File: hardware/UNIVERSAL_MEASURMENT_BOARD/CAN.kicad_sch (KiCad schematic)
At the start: 12 parts, among them U5 ADM3055EBRIZ-RL

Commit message: continued
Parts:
- removed FB2: FerriteBead_Small, symbol Device:FerriteBead_Small
- added C61: 47uF, symbol Device:C_Small
- added C67: 4.7nF/Y2, Samacsys:CAPC5728X280N, symbol Samacsys_kicad_sym:S252B222K502CT
- added FB1, FB3, FB4: 2K@100MHz, symbol Device:FerriteBead_Small
- added TP1: C5V, symbol Connector:TestPoint
- added TP2: C3V, symbol Connector:TestPoint
- C58: renamed from C13; value 220nF -> 47uF
- C59: renamed from C14; value 10uF -> 47uF
- C60: renamed from C17; value 10uF -> 47uF
- FB2: renamed from FB1; value FerriteBead_Small -> 2K@100MHz
- R14: renamed from R2; value R -> 100kR
- renumbered C18 to C62, C19 to C63, C20 to C64, C15 to C65, C16 to C66, U5 to U14
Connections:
- net +3V3: now also FB3.2; no longer C64.1, U14.4 (VIO)
- net +5V: now also FB1.2; no longer C62.1, U14.3 (VCC)
- net BUS_GND: now also C67.1, FB4.2
- net GND: now also U14.9 (AUXIN), C61.2, C67.2
- net at C58.2, U14.18 (GNDISO), U14.20 (GNDISO_2): now also FB4.1
- net CAN_STB: now reaches U14.8 (STBY)
- new net: C61.1, C62.1, FB1.1, TP1.1, U14.3 (VCC)
- new net: C64.1, FB3.1, TP2.1, U14.4 (VIO)
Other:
- note added: "ISOLATED"
- note added: "NON ISOLATED"
- note removed: "Co z VISO"
- company: (none) -> PUT Motorsport Formula Student team
- title: (none) -> Universal Measurment Board
- moved on the sheet: C58, C59, C60, C62, C63, C64, C65, C66, FB2, R14

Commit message: final schematic review corrections
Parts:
- added TP3: CVISO, symbol Connector:TestPoint
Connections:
- net VISO: now also TP3.1
- net +5V renamed +5V0A
- net RX renamed CAN_RX
- net TX renamed CAN_TX
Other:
- moved on the sheet: C58, C59, C60, C61, C62, C63, C64, C65, C66, C67, FB1, FB2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

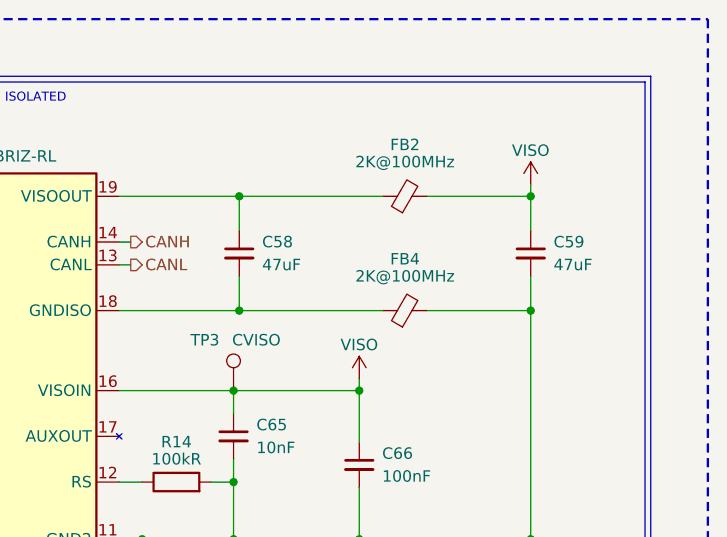
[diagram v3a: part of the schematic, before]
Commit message: added footprints
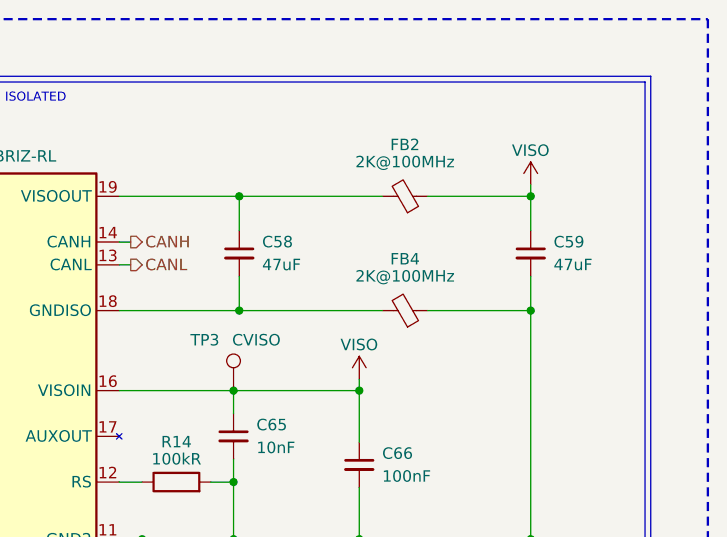
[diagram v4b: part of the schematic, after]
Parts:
- C58, C59, C60, C61, C62, C63, C64, C65, C66: footprint (none) -> Capacitor_SMD:C_0603_1608Metric
- C67: footprint Samacsys:CAPC5728X280N -> S252B222K502CT:CAPC5728X280N
- FB1, FB2, FB3, FB4: footprint (none) -> Inductor_SMD:L_0805_2012Metric
- R14: footprint (none) -> Resistor_SMD:R_0603_1608Metric
- TP1, TP2, TP3: footprint (none) -> TestPoint:TestPoint_Pad_D1.5mm
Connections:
- net BUS_GND: now also FB4.1; no longer FB4.2
- net VISO: now also FB2.1; no longer FB2.2
- net at C58.1, U14.19 (VISOOUT): now also FB2.2; no longer FB2.1
- net at C58.2, U14.18 (GNDISO), U14.20 (GNDISO_2): now also FB4.2; no longer FB4.1
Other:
- company: PUT Motorsport Formula Student team -> PUT Motorsport Formula Student Team
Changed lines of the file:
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@@
 		(title "Universal Measurment Board")
 		(date "2026-02-02")
-		(rev "1.7.14")
-		(company "PUT Motorsport Formula Student team")
+		(rev "1.7.15")
+		(company "PUT Motorsport Formula Student Team")
 		(comment 1 "Designed by Marcin Trzmiel under")
 	)
@@
 			)
 		)
-		(property "Footprint" ""
+		(property "Footprint" "Capacitor_SMD:C_0603_1608Metric"
 			(at 94.615 88.265 0)
 			(effects
@@
 			)
 		)
-		(property "Footprint" ""
+		(property "Footprint" "TestPoint:TestPoint_Pad_D1.5mm"
 			(at 146.05 69.215 0)
 			(effects
@@
 			)
 		)
-		(property "Footprint" ""
+		(property "Footprint" "TestPoint:TestPoint_Pad_D1.5mm"
 			(at 129.54 76.835 0)
 			(effects
@@
 	)
 	(symbol
-		(lib_id "Device:FerriteBead_Small")
-		(at 76.2 69.215 270)
-		(unit 1)
-		(exclude_from_sim no)
-		(in_bom yes)
-		(on_board yes)
-		(dnp no)
-		(property "Reference" "FB1"
-			(at 76.2 73.025 90)
-			(effects
-				(font
-					(size 1.27 1.27)
-				)
-			)
-		)
-		(property "Value" "2K@100MHz"
-			(at 76.2 74.93 90)
-			(effects
-				(font
-					(size 1.27 1.27)
-				)
-			)
-		)
-		(property "Footprint" ""
-			(at 76.2 67.437 90)
-			(effects
-				(font
-					(size 1.27 1.27)
-				)
-				(hide yes)
-			)
-		)
-		(property "Datasheet" "~"
-			(at 76.2 69.215 0)
-			(effects
-				(font
-					(size 1.27 1.27)
-				)
-				(hide yes)
-			)
-		)
-		(property "Description" "Ferrite bead, small symbol"
-			(at 76.2 69.215 0)
-			(effects
-				(font
-					(size 1.27 1.27)
-				)
-				(hide yes)
-			)
-		)
-		(pin "2"
-		)
-		(pin "1"
-		)
-		(instances
-			(project "UNIVERSAL_MEASURMENT_BOARD"
-				(path "/92c00310-4384-4ef3-9368-efad75526047/007c1dd5-a7d9-42e3-b7c2-f5a2b9d94f0b"
-					(reference "FB1")
-					(unit 1)
-				)
-			)
-		)
-	)
-	(symbol
 		(lib_id "Samacsys_kicad_sym:S252B222K502CT")
 		(at 164.465 118.745 180)
@@
 			)
 		)
-		(property "Footprint" "Samacsys:CAPC5728X280N"
+		(property "Footprint" "S252B222K502CT:CAPC5728X280N"
 			(at 155.575 22.555 0)
 			(effects
@@
 			)
 		)
-		(property "Datasheet" ""
+		(property "Datasheet" "https://4donline.ihs.com/images/VipMasterIC/IC/WATC/WATC-S-A0011771687/WATC-S-A0011771687-1.pdf?hkey=CECEF36DEECDED6468708AAF2E19C0C6"
 			(at 155.575 -77.445 0)
 			(effects
@@
 			)
 		)
-		(property "Footprint" ""
+		(property "Footprint" "Capacitor_SMD:C_0603_1608Metric"
 			(at 193.04 75.565 0)
 			(effects
@@
 	)
 	(symbol
-		(lib_id "Device:FerriteBead_Small")
-		(at 211.455 69.215 90)
-		(unit 1)
-		(exclude_from_sim no)
-		(in_bom yes)
-		(on_board yes)
-		(dnp no)
-		(property "Reference" "FB2"
-			(at 211.455 63.5 90)
-			(effects
-				(font
-					(size 1.27 1.27)
-				)
-			)
-		)
-		(property "Value" "2K@100MHz"
-			(at 211.455 65.405 90)
-			(effects
-				(font
-					(size 1.27 1.27)
-				)
-			)
-		)
-		(property "Footprint" ""
-			(at 211.455 70.993 90)
-			(effects
-				(font
-					(size 1.27 1.27)
-				)
-				(hide yes)
-			)
-		)
-		(property "Datasheet" "~"
-			(at 211.455 69.215 0)
-			(effects
-				(font
-					(size 1.27 1.27)
-				)
-				(hide yes)
-			)
-		)
-		(property "Description" "Ferrite bead, small symbol"
-			(at 211.455 69.215 0)
-			(effects
-				(font
-					(size 1.27 1.27)
-				)
-				(hide yes)
-			)
-		)
-		(pin "2"
-		)
-		(pin "1"
-		)
-		(instances
-			(project ""
-				(path "/92c00310-4384-4ef3-9368-efad75526047/007c1dd5-a7d9-42e3-b7c2-f5a2b9d94f0b"
-					(reference "FB2")
-					(unit 1)
-				)
-			)
-		)
-	)
-	(symbol
 		(lib_id "Device:C_Small")
 		(at 225.425 75.565 0)
@@
 			)
 		)
-		(property "Footprint" ""
+		(property "Footprint" "Capacitor_SMD:C_0603_1608Metric"
 			(at 225.425 75.565 0)
 			(effects
@@
 			)
 		)
-		(property "Footprint" ""
+		(property "Footprint" "Capacitor_SMD:C_0603_1608Metric"
 			(at 192.405 95.885 0)
 			(effects
@@
 	(symbol
 		(lib_id "Device:FerriteBead_Small")
-		(at 211.455 81.915 90)
+		(at 211.455 81.915 270)
+		(mirror x)
 		(unit 1)
 		(exclude_from_sim no)
@@
 			)
 		)
-		(property "Footprint" ""
+		(property "Footprint" "Inductor_SMD:L_0805_2012Metric"
 			(at 211.455 83.693 90)
 			(effects
@@
 			)
 		)
-		(property "Datasheet" "~"
+		(property "Datasheet" "https://www.mouser.pl/ProductDetail/Fair-Rite/2508052027Y1?qs=paL1wOLBYNcCgyNDp2sTMQ%3D%3D"
 			(at 211.455 81.915 0)
 			(effects
@@
 			)
 		)
-		(property "Footprint" ""
+		(property "Footprint" "Capacitor_SMD:C_0603_1608Metric"
 			(at 125.095 92.075 0)
 			(effects
@@
 			)
 		)
-		(property "Footprint" ""
+		(property "Footprint" "Resistor_SMD:R_0603_1608Metric"
 			(at 186.055 102.743 90)
 			(effects
@@
 			)
 		)
-		(property "Footprint" ""
+		(property "Footprint" "Inductor_SMD:L_0805_2012Metric"
 			(at 117.475 75.057 90)
 			(effects
@@
 			)
 		)
-		(property "Datasheet" "~"
+		(property "Datasheet" "https://www.mouser.pl/ProductDetail/Fair-Rite/2508052027Y1?qs=paL1wOLBYNcCgyNDp2sTMQ%3D%3D"
 			(at 117.475 76.835 0)
 			(effects
@@
 			)
 		)
-		(property "Footprint" ""
+		(property "Footprint" "Capacitor_SMD:C_0603_1608Metric"
 			(at 206.375 99.06 0)
 			(effects
@@
 			)
 		)
-		(property "Footprint" ""
+		(property "Footprint" "Capacitor_SMD:C_0603_1608Metric"
 			(at 68.58 88.265 0)
 			(effects
@@
 	)
 	(symbol
+		(lib_id "Device:FerriteBead_Small")
+		(at 211.455 69.215 270)
+		(mirror x)
+		(unit 1)
+		(exclude_from_sim no)
+		(in_bom yes)
+		(on_board yes)
+		(dnp no)
+		(property "Reference" "FB2"
+			(at 211.455 63.5 90)
+			(effects
+				(font
+					(size 1.27 1.27)
+				)
+			)
+		)
+		(property "Value" "2K@100MHz"
+			(at 211.455 65.405 90)
+			(effects
+				(font
+					(size 1.27 1.27)
+				)
+			)
+		)
+		(property "Footprint" "Inductor_SMD:L_0805_2012Metric"
+			(at 211.455 70.993 90)
+			(effects
+				(font
+					(size 1.27 1.27)
+				)
+				(hide yes)
+			)
+		)
+		(property "Datasheet" "https://www.mouser.pl/ProductDetail/Fair-Rite/2508052027Y1?qs=paL1wOLBYNcCgyNDp2sTMQ%3D%3D"
+			(at 211.455 69.215 0)
+			(effects
+				(font
+					(size 1.27 1.27)
+				)
+				(hide yes)
+			)
+		)
+		(property "Description" "Ferrite bead, small symbol"
+			(at 211.455 69.215 0)
+			(effects
+				(font
+					(size 1.27 1.27)
+				)
+				(hide yes)
+			)
+		)
+		(pin "2"
+		)
+		(pin "1"
+		)
+		(instances
+			(project "UNIVERSAL_MEASURMENT_BOARD"
+				(path "/92c00310-4384-4ef3-9368-efad75526047/007c1dd5-a7d9-42e3-b7c2-f5a2b9d94f0b"
+					(reference "FB2")
+					(unit 1)
+				)
+			)
+		)
+	)
+	(symbol
+		(lib_id "Device:FerriteBead_Small")
+		(at 76.2 69.215 270)
+		(unit 1)
+		(exclude_from_sim no)
+		(in_bom yes)
+		(on_board yes)
+		(dnp no)
+		(property "Reference" "FB1"
+			(at 76.2 73.025 90)
+			(effects
+				(font
+					(size 1.27 1.27)
+				)
+			)
+		)
+		(property "Value" "2K@100MHz"
+			(at 76.2 74.93 90)
+			(effects
+				(font
+					(size 1.27 1.27)
+				)
+			)
+		)
+		(property "Footprint" "Inductor_SMD:L_0805_2012Metric"
+			(at 76.2 67.437 90)
+			(effects
+				(font
+					(size 1.27 1.27)
+				)
+				(hide yes)
+			)
+		)
+		(property "Datasheet" "https://www.mouser.pl/ProductDetail/Fair-Rite/2508052027Y1?qs=paL1wOLBYNcCgyNDp2sTMQ%3D%3D"
+			(at 76.2 69.215 0)
+			(effects
+				(font
+					(size 1.27 1.27)
+				)
+				(hide yes)
+			)
+		)
+		(property "Description" "Ferrite bead, small symbol"
+			(at 76.2 69.215 0)
+			(effects
+				(font
+					(size 1.27 1.27)
+				)
+				(hide yes)
+			)
+		)
+		(pin "2"
+		)
+		(pin "1"
+		)
+		(instances
+			(project "UNIVERSAL_MEASURMENT_BOARD"
+				(path "/92c00310-4384-4ef3-9368-efad75526047/007c1dd5-a7d9-42e3-b7c2-f5a2b9d94f0b"
+					(reference "FB1")
+					(unit 1)
+				)
+			)
+		)
+	)
+	(symbol
 		(lib_id "Connector:TestPoint")
 		(at 192.405 90.805 0)
@@
 			)
 		)
-		(property "Footprint" ""
+		(property "Footprint" "TestPoint:TestPoint_Pad_D1.5mm"
 			(at 197.485 90.805 0)
 			(effects
@@
 			)
 		)
-		(property "Footprint" ""
+		(property "Footprint" "Capacitor_SMD:C_0603_1608Metric"
 			(at 109.855 92.075 0)
 			(effects
@@
 			)
 		)
-		(property "Footprint" ""
+		(property "Footprint" "Capacitor_SMD:C_0603_1608Metric"
 			(at 83.82 88.265 0)
 			(effects

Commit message: first outcom of pcb design
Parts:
- removed TP1: C5V, TestPoint:TestPoint_Pad_D1.5mm, symbol Connector:TestPoint
- removed TP2: C3V, TestPoint:TestPoint_Pad_D1.5mm, symbol Connector:TestPoint
- C65: renamed from C60; footprint Capacitor_SMD:C_0603_1608Metric -> REST:C_0603_1608Metric
- C66: renamed from C61; footprint Capacitor_SMD:C_0603_1608Metric -> REST:C_0603_1608Metric
- C67: renamed from C62; footprint Capacitor_SMD:C_0603_1608Metric -> REST:C_0603_1608Metric
- C68: renamed from C63; footprint Capacitor_SMD:C_0603_1608Metric -> REST:C_0603_1608Metric
- C69: renamed from C64; footprint Capacitor_SMD:C_0603_1608Metric -> REST:C_0603_1608Metric
- C71: renamed from C65; footprint Capacitor_SMD:C_0603_1608Metric -> REST:C_0603_1608Metric
- C72: renamed from C58; footprint Capacitor_SMD:C_0603_1608Metric -> REST:C_0603_1608Metric
- C73: renamed from C66; footprint Capacitor_SMD:C_0603_1608Metric -> REST:C_0603_1608Metric
- C74: renamed from C59; footprint Capacitor_SMD:C_0603_1608Metric -> REST:C_0603_1608Metric
- FB1, FB4: footprint Inductor_SMD:L_0805_2012Metric -> REST:L_0805_2012Metric
- FB2: renamed from FB3; footprint Inductor_SMD:L_0805_2012Metric -> REST:L_0805_2012Metric
- FB3: renamed from FB2; footprint Inductor_SMD:L_0805_2012Metric -> REST:L_0805_2012Metric
- R19: renamed from R14; footprint Resistor_SMD:R_0603_1608Metric -> REST:R_0603_1608Metric
- TP15: renamed from TP3; footprint TestPoint:TestPoint_Pad_D1.5mm -> REST:TestPoint_Pad_D1.5mm
- renumbered C67 to C70, U14 to U18
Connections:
- net BUS_GND renamed GND_ISO

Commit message: Review fixes
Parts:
- removed U18: ADM3055EBRIZ-RL, SOIC127P1030X264-20N, symbol ADM3055EBRIZ-RL:ADM3055EBRIZ-RL
- added U18: ADM3057EBRWZ, SOIC127P1032X265-20N, symbol ADM3057EBRWZ:ADM3057EBRWZ
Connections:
- net CANH: now also U18.14 (CANH)
- net CANL: now also U18.13 (CANL)
- net CAN_RX: now also U18.5 (RXD)
- net CAN_STB: now also U18.8 (STBY)
- net CAN_TX: now also U18.7 (TXD)
- net GND: now also U18.1 (GND1), U18.10 (GND1_3), U18.2 (GND1_2), U18.9 (AUXIN)
- net GND_ISO: now also U18.11 (GND2), U18.15 (GND2_2)
- net VISO: now also U18.16 (VISOIN)
- net at C66.1, C67.1, FB1.1: now also U18.3 (VCC)
- net at C72.1, FB3.2: now also U18.19 (VISOOUT)
- net at C72.2, FB4.2: now also U18.18 (GNDISO), U18.20 (GNDISO_2)
- net at C69.1, FB2.1: now also U18.4 (VIO)
- net at R19.1: now also U18.12 (RS)
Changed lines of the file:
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@@
+	)
+	(symbol
+		(lib_name "ADM3057EBRWZ_2")
+		(lib_id "ADM3057EBRWZ:ADM3057EBRWZ")
+		(at 164.465 88.265 0)
+		(unit 1)
+		(body_style 1)
+		(exclude_from_sim no)
+		(in_bom yes)
+		(on_board yes)
+		(in_pos_files yes)
+		(dnp no)
+		(fields_autoplaced yes)
+		(property "Reference" "U18"
+			(at 164.465 62.23 0)
+			(show_name no)
+			(do_not_autoplace no)
+			(effects
+				(font
+					(size 1.27 1.27)
+				)
+			)
+		)
+		(property "Value" "ADM3057EBRWZ"
+			(at 164.465 64.77 0)
+			(show_name no)
+			(do_not_autoplace no)
+			(effects
+				(font
+					(size 1.27 1.27)
+				)
+			)
+		)
+		(property "Footprint" "SOIC127P1032X265-20N"
+			(at 196.215 183.185 0)
+			(hide yes)
+			(show_name no)
+			(do_not_autoplace no)
+			(effects
+				(font
+					(size 1.27 1.27)
+				)
+				(justify left top)
+			)
+		)
+		(property "Datasheet" "https://www.analog.com/ADM3057E/datasheet"
+			(at 196.215 283.185 0)
+			(hide yes)
+			(show_name no)
+			(do_not_autoplace no)
+			(effects
+				(font
+					(size 1.27 1.27)
+				)
+				(justify left top)
+			)
+		)
+		(property "Description" "3 kV rms, Signal and Power Isolated, CAN Transceiver for CAN FD"
+			(at 164.465 22.733 0)
+			(hide yes)
+			(show_name no)
+			(do_not_autoplace no)
+			(effects
+				(font
+					(size 1.27 1.27)
+				)
+			)
+		)
+		(property "Height" "2.65"
+			(at 196.215 483.185 0)
+			(hide yes)
+			(show_name no)
+			(do_not_autoplace no)
+			(effects
+				(font
+					(size 1.27 1.27)
+				)
+				(justify left top)
+			)
+		)
+		(property "Mouser Part Number" "584-ADM3057EBRWZ"
+			(at 196.215 583.185 0)
+			(hide yes)
+			(show_name no)
+			(do_not_autoplace no)
+			(effects
+				(font
+					(size 1.27 1.27)
+				)
+				(justify left top)
+			)
+		)
+		(property "Mouser Price/Stock" "https://www.mouser.co.uk/ProductDetail/Analog-Devices/ADM3057EBRWZ?qs=PqoDHHvF649%2FWAcdgp0Vvw%3D%3D"
+			(at 196.215 683.185 0)
+			(hide yes)
+			(show_name no)
+			(do_not_autoplace no)
+			(effects
+				(font
+					(size 1.27 1.27)
+				)
+				(justify left top)
+			)
+		)
+		(property "Manufacturer_Name" "Analog Devices"
+			(at 196.215 783.185 0)
+			(hide yes)
+			(show_name no)
+			(do_not_autoplace no)
+			(effects
+				(font
+					(size 1.27 1.27)
+				)
+				(justify left top)
+			)
+		)
+		(property "Manufacturer_Part_Number" "ADM3057EBRWZ"
+			(at 196.215 883.185 0)
+			(hide yes)
+			(show_name no)
+			(do_not_autoplace no)
+			(effects
+				(font
+					(size 1.27 1.27)
+				)
+				(justify left top)
+			)
+		)
+		(pin "5"
+		)
+		(pin "3"
+		)
+		(pin "1"
+		)
+		(pin "2"
+		)
+		(pin "4"
+		)
+		(pin "8"
+		)
+		(pin "9"
+		)
+		(pin "6"
+		)
+		(pin "15"
+		)
+		(pin "17"
+		)
+		(pin "18"
+		)
+		(pin "14"
+		)
+		(pin "11"
+		)
+		(pin "13"
+		)
+		(pin "10"
+		)
+		(pin "12"
+		)
+		(pin "19"
+		)
+		(pin "16"
+		)
+		(pin "20"
+		)
+		(pin "7"
+		)
+		(instances
+			(project "UNIVERSAL_MEASURMENT_BOARD"
+				(path "/92c00310-4384-4ef3-9368-efad75526047/007c1dd5-a7d9-42e3-b7c2-f5a2b9d94f0b"
+					(reference "U18")
+					(unit 1)
+				)
+			)
+		)
 	)
 	(symbol
@@
 					(unit 1)
 				)
-			)
-		)
-	)
-	(symbol
-		(lib_id "ADM3055EBRIZ-RL:ADM3055EBRIZ-RL")
-		(at 164.465 88.265 0)
-		(unit 1)
-		(body_style 1)
-		(exclude_from_sim no)
-		(in_bom yes)
-		(on_board yes)
-		(in_pos_files yes)
-		(dnp no)
-		(fields_autoplaced yes)
-		(property "Reference" "U18"
-			(at 164.465 62.23 0)
-			(show_name no)
-			(do_not_autoplace no)
-			(effects
-				(font
-					(size 1.27 1.27)
-				)
-			)
-		)
-		(property "Value" "ADM3055EBRIZ-RL"
-			(at 164.465 64.77 0)
-			(show_name no)
-			(do_not_autoplace no)
-			(effects
-				(font
-					(size 1.27 1.27)
-				)
-			)
-		)
-		(property "Footprint" "SOIC127P1030X264-20N"
-			(at 196.215 175.565 0)
-			(hide yes)
-			(show_name no)
-			(do_not_autoplace no)
-			(effects
-				(font
-					(size 1.27 1.27)
-				)
-				(justify left top)
-			)
-		)
-		(property "Datasheet" "https://www.analog.com/media/en/technical-documentation/data-sheets/ADM3055E-3057E.pdf"
-			(at 196.215 275.565 0)
-			(hide yes)
-			(show_name no)
-			(do_not_autoplace no)
-			(effects
-				(font
-					(size 1.27 1.27)
-				)
-				(justify left top)
-			)
-		)
-		(property "Description" "CAN Interface IC 5kV isoPower Isolated CAN-FD Transceiver"
-			(at 164.465 48.387 0)
-			(hide yes)
-			(show_name no)
-			(do_not_autoplace no)
-			(effects
-				(font
-					(size 1.27 1.27)
-				)
-			)
-		)
-		(property "Height" "2.64"
-			(at 196.215 475.565 0)
-			(hide yes)
-			(show_name no)
-			(do_not_autoplace no)
-			(effects
-				(font
-					(size 1.27 1.27)
-				)
-				(justify left top)
-			)
-		)
-		(property "Mouser Part Number" "584-ADM3055EBRIZ-RL"
-			(at 196.215 575.565 0)
-			(hide yes)
-			(show_name no)
-			(do_not_autoplace no)
-			(effects
-				(font
-					(size 1.27 1.27)
-				)
-				(justify left top)
-			)
-		)
-		(property "Mouser Price/Stock" "https://www.mouser.co.uk/ProductDetail/Analog-Devices/ADM3055EBRIZ-RL?qs=qSfuJ%252Bfl%2Fd7r0f9T4vdNWQ%3D%3D"
-			(at 196.215 675.565 0)
-			(hide yes)
-			(show_name no)
-			(do_not_autoplace no)
-			(effects
-				(font
-					(size 1.27 1.27)
-				)
-				(justify left top)
-			)
-		)
-		(property "Manufacturer_Name" "Analog Devices"
-			(at 196.215 775.565 0)
-			(hide yes)
-			(show_name no)
-			(do_not_autoplace no)
-			(effects
-				(font
-					(size 1.27 1.27)
-				)
-				(justify left top)
-			)
-		)
-		(property "Manufacturer_Part_Number" "ADM3055EBRIZ-RL"
-			(at 196.215 875.565 0)
-			(hide yes)
-			(show_name no)
-			(do_not_autoplace no)
-			(effects
-				(font
-					(size 1.27 1.27)
-				)
-				(justify left top)
-			)
-		)
-		(pin "16"
-		)
-		(pin "2"
-		)
-		(pin "5"
-		)
-		(pin "14"
-		)
-		(pin "20"
-		)
-		(pin "3"
-		)
-		(pin "7"
-		)
-		(pin "19"
-		)
-		(pin "8"
-		)
-		(pin "10"
-		)
-		(pin "9"
-		)
-		(pin "13"
-		)
-		(pin "1"
-		)
-		(pin "4"
-		)
-		(pin "18"
-		)
-		(pin "6"
-		)
-		(pin "12"
-		)
-		(pin "11"
-		)
-		(pin "17"
-		)
-		(pin "15"
-		)
-		(instances
-			(project "UNIVERSAL_MEASURMENT_BOARD"
-				(path "/92c00310-4384-4ef3-9368-efad75526047/007c1dd5-a7d9-42e3-b7c2-f5a2b9d94f0b"
-					(reference "U18")
-					(unit 1)
-				)
